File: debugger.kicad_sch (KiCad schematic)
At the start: 35 parts, among them SW3 SW-434153017835‎, U1 W25Q16JVUXIQ_TR, U11 TPS22919, U5 RP2040, U8 TS5A3166DCKR, U9 TC7PZ14FU, Y1 Crystal_GND24

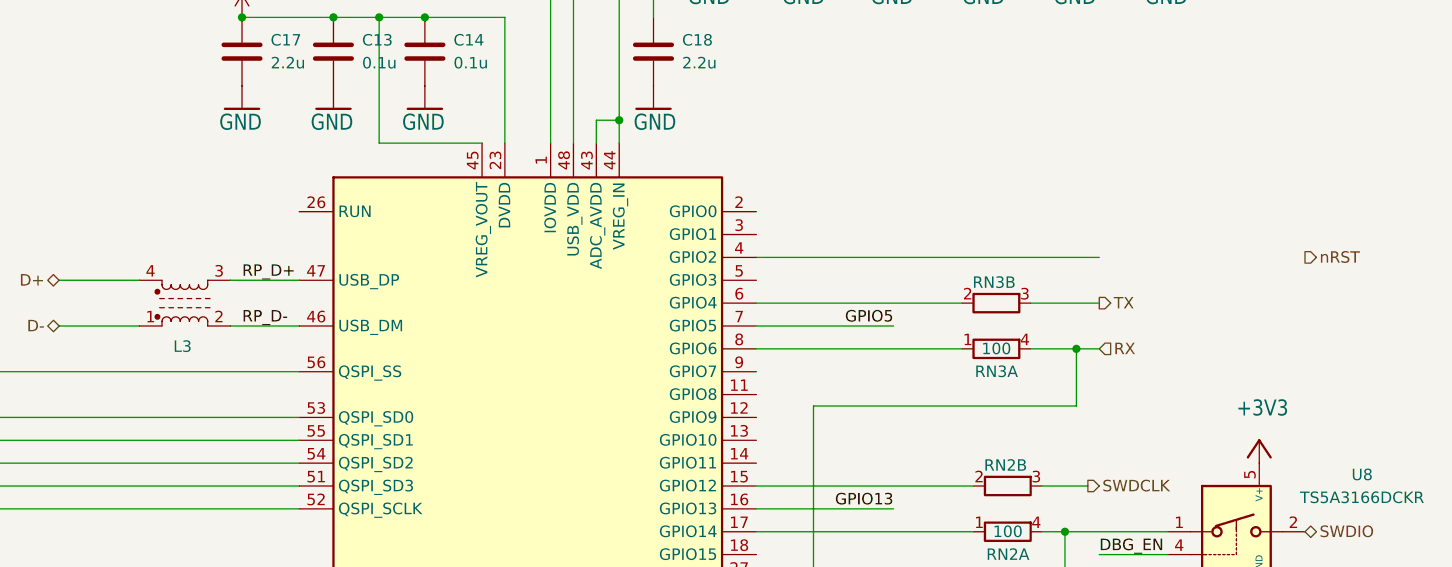
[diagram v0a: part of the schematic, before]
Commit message: Fixing error in schematic w/ nRST
nRST on debugger should not (and is not) connected to the nRST signal to the processor. Cleaning up schematic to clear up confusion around that. PCB routing remains unchanged.
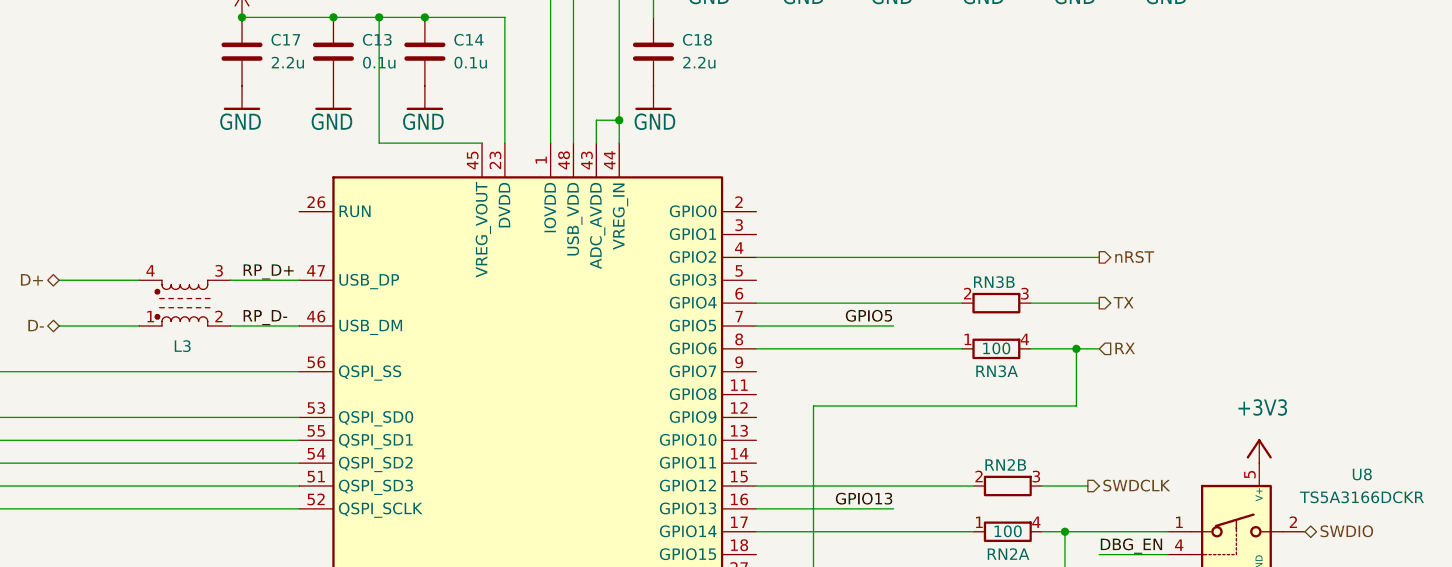
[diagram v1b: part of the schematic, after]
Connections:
- net nRST: now also U5.4 (GPIO2)

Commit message: Updating parts:
1. Button change
2. USB change
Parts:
- SW3: footprint Circuit Dojo:WOLFF-DEN_SW-EVP-AA402W -> Button_Switch_SMD:SW_SPST_B3U-1000P
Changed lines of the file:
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@@
 			)
 		)
-		(property "Footprint" "Circuit Dojo:WOLFF-DEN_SW-EVP-AA402W"
+		(property "Footprint" "Button_Switch_SMD:SW_SPST_B3U-1000P"
 			(at 64.77 132.08 0)
 			(effects

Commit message: Adding variant control
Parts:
- C12, C13, C14, C15, C16, C17, C18, C19, C20, C21, C22, C47, C5, C6, C7, C9, D2, L3, R13, R14, R6, R7, R9, RN2, RN3, RN4, SW3, U1, U11, U5, U8, U9, Y1: Var (none) -> Variant Standard(+!) Cptel(-!)
- TP3, TP4: now left out of the parts list
